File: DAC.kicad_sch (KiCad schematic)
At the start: 1 part, among them U401 MCP4728T-E_UN

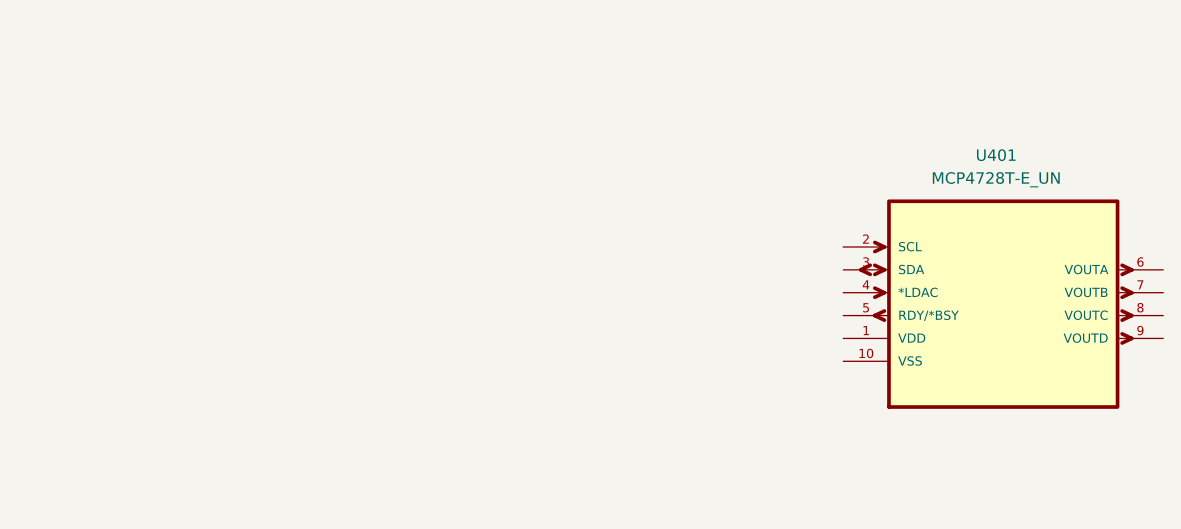
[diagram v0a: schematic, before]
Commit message: finished ADC side, may add some additional bare channels, started DAC part and need to add the tca0372 amplifier or think about it
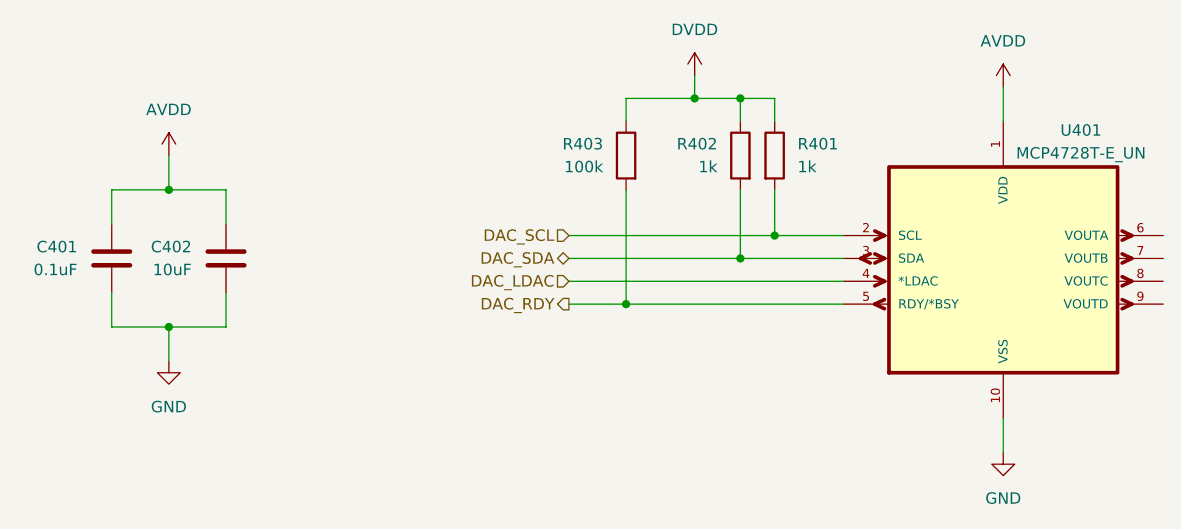
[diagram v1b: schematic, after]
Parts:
- added C401: 0.1uF, symbol Device:C
- added C402: 10uF, symbol Device:C
- added R401, R402: 1k, symbol Device:R
- added R403: 100k, symbol Device:R
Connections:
- net AVDD: now reaches U401.1 (VDD)
- net AVDD: now also C401.1, C402.1
- net GND: now reaches U401.10 (VSS)
- net GND: now also C401.2, C402.2
- net DAC_SCL: now reaches U401.2 (SCL)
- net DAC_SCL: now also R401.2
- net DAC_SDA: now reaches U401.3 (SDA)
- net DAC_SDA: now also R402.2
- net DAC_LDAC: now reaches U401.4 (*LDAC)
- net DAC_RDY: now reaches U401.5 (RDY/*BSY)
- net DAC_RDY: now also R403.2
- new net DVDD: R401.1, R402.1, R403.1
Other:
- moved on the sheet: U401

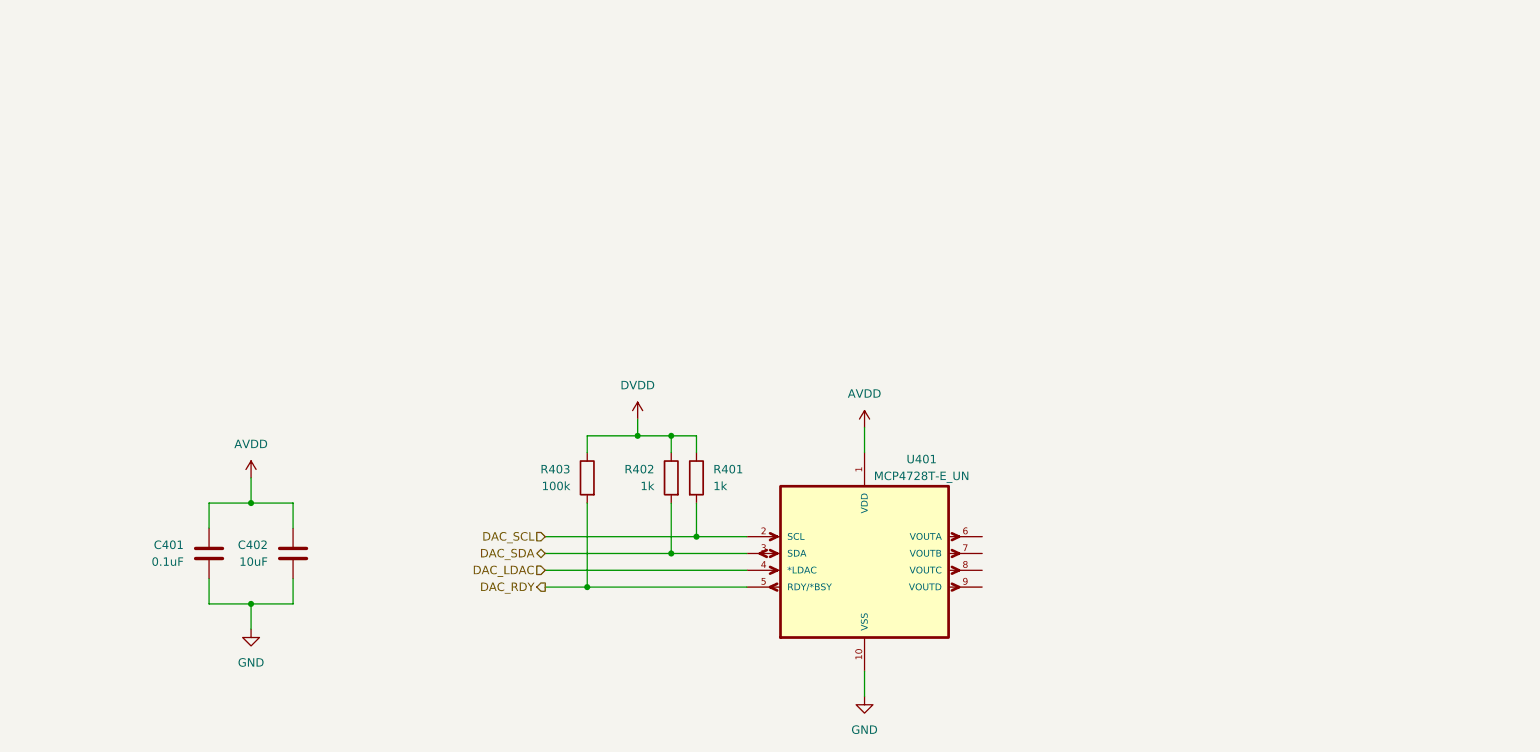
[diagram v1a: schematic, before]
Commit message: 80% done, maybe add more AINs, finish the power circuit and add system & block diagrams
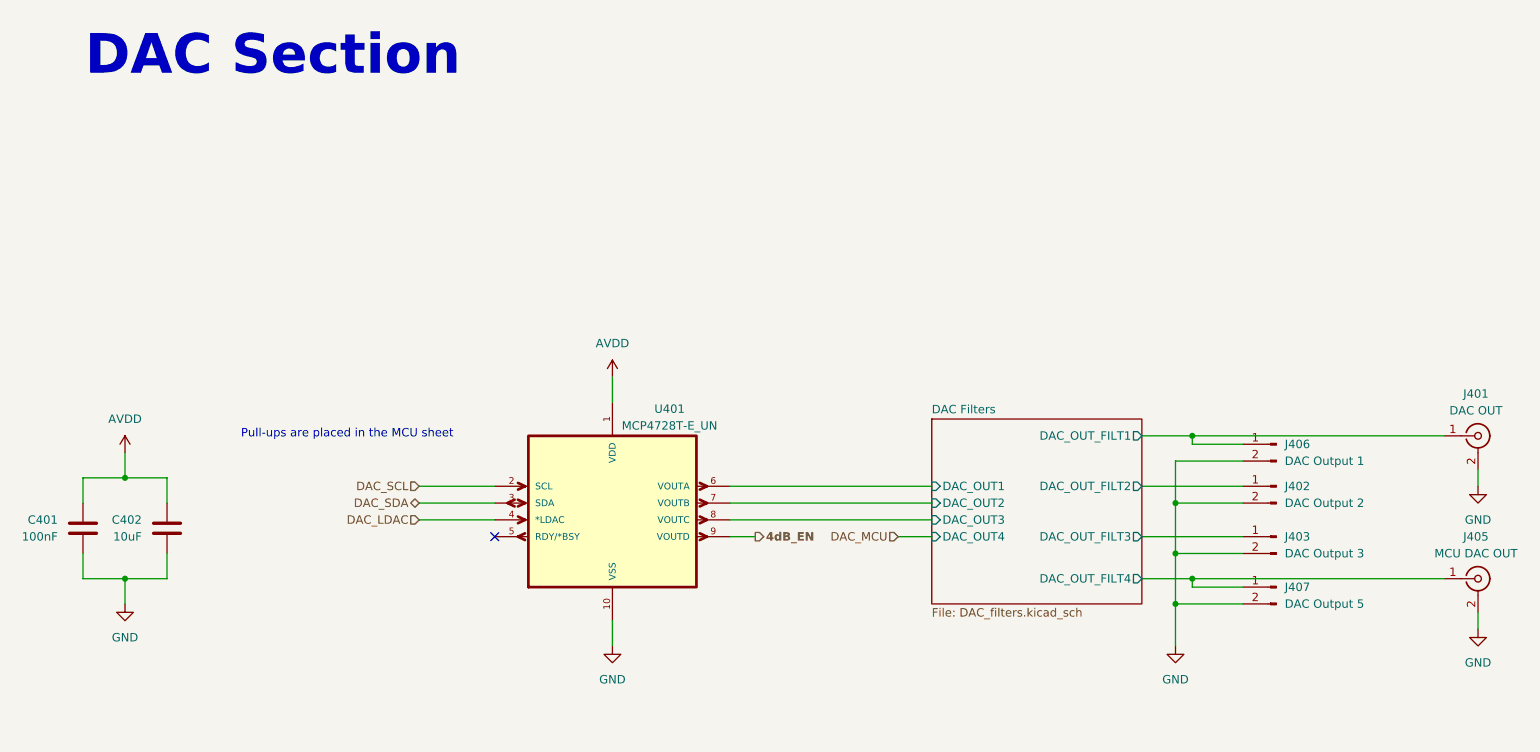
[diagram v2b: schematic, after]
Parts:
- removed R401, R402: 1k, symbol Device:R
- removed R403: 100k, symbol Device:R
- added J401: DAC OUT, symbol Connector:Conn_Coaxial
- added J402: DAC Output 2, symbol Connector:Conn_01x02_Pin
- added J403: DAC Output 3, symbol Connector:Conn_01x02_Pin
- added J405: MCU DAC OUT, symbol Connector:Conn_Coaxial
- added J406: DAC Output 1, symbol Connector:Conn_01x02_Pin
- added J407: DAC Output 5, symbol Connector:Conn_01x02_Pin
- C401: value 0.1uF -> 100nF
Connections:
- net GND: now also J401.2 (Ext), J402.2 (Pin_2), J403.2 (Pin_2), J405.2 (Ext), J406.2 (Pin_2), J407.2 (Pin_2)
- net DAC Filters/DAC_OUT1: now reaches U401.6 (VOUTA)
- net DAC Filters/DAC_OUT2: now reaches U401.7 (VOUTB)
- net DAC Filters/DAC_OUT3: now reaches U401.8 (VOUTC)
- net 4dB_EN: now reaches U401.9 (VOUTD)
- net DAC_RDY: no longer names the net of U401.5 (RDY/*BSY)
- new net DAC Filters/DAC_OUT_FILT1: J401.1 (In), J406.1 (Pin_1)
- new net DAC Filters/DAC_OUT_FILT2: J402.1 (Pin_1)
- new net DAC Filters/DAC_OUT_FILT3: J403.1 (Pin_1)
- new net DAC Filters/DAC_OUT_FILT4: J405.1 (In), J407.1 (Pin_1)
- no-connect marks 0 -> 1
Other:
- added sheet DAC Filters (DAC_filters.kicad_sch)
- note added: "DAC Section"
- note added: "Pull-ups are placed in the MCU sheet"
- moved on the sheet: C401, C402, U401

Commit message: finished individual block placement and started integrating, might need to change the AFEs length
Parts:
- C401: footprint (none) -> Capacitor_SMD:C_0603_1608Metric; MPN (none) -> 0603B104M250CT
- C402: footprint (none) -> Capacitor_SMD:C_0603_1608Metric; MPN (none) -> CL10A106MP8NNNC
- J401, J405: footprint (none) -> DOSIN-801-0083:CONN4_DOSIN-801_DOS; MPN (none) -> DOSIN-801-0083
- J402, J403, J406, J407: footprint (none) -> Connector_PinHeader_2.54mm:PinHeader_1x02_P2.54mm_Vertical; now not fitted
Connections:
- net 4dB_EN: no longer names the net of U401.9 (VOUTD)
- no-connect marks 1 -> 2
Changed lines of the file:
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@@
+	)
+	(no_connect
+		(at 120.65 95.25)
 	)
 	(no_connect
@@
 		(pts
 			(xy 120.65 92.71) (xy 151.13 92.71)
-		)
-		(stroke
-			(width 0)
-			(type default)
-		)
-	)
-	(wire
-		(pts
-			(xy 120.65 95.25) (xy 124.46 95.25)
 		)
 		(stroke
@@
 			)
 			(justify right)
-		)
-	)
-	(hierarchical_label "4dB_EN"
-		(shape output)
-		(at 124.46 95.25 0)
-		(effects
-			(font
-				(size 1.27 1.27)
-				(thickness 0.254)
-				(bold yes)
-			)
-			(justify left)
 		)
 	)
@@
 			)
 		)
-		(property "Footprint" ""
+		(property "Footprint" "DOSIN-801-0083:CONN4_DOSIN-801_DOS"
 			(at 233.68 101.6 0)
 			(effects
@@
 		)
 		(property "Description" "coaxial connector (BNC, SMA, SMB, SMC, Cinch/RCA, LEMO, ...)"
+			(at 233.68 101.6 0)
+			(effects
+				(font
+					(size 1.27 1.27)
+				)
+				(hide yes)
+			)
+		)
+		(property "MPN" "DOSIN-801-0083"
 			(at 233.68 101.6 0)
 			(effects
@@
 		(in_bom yes)
 		(on_board yes)
-		(dnp no)
+		(dnp yes)
 		(fields_autoplaced yes)
 		(property "Reference" "J407"
@@
 			)
 		)
-		(property "Footprint" ""
+		(property "Footprint" "Connector_PinHeader_2.54mm:PinHeader_1x02_P2.54mm_Vertical"
 			(at 203.2 102.87 0)
 			(effects
@@
 			)
 		)
-		(property "Footprint" ""
+		(property "Footprint" "Capacitor_SMD:C_0603_1608Metric"
 			(at 23.8252 97.79 0)
 			(effects
@@
 		)
 		(property "Description" "100nF 0603"
+			(at 22.86 93.98 0)
+			(effects
+				(font
+					(size 1.27 1.27)
+				)
+				(hide yes)
+			)
+		)
+		(property "MPN" "0603B104M250CT"
 			(at 22.86 93.98 0)
 			(effects
@@
 		(in_bom yes)
 		(on_board yes)
-		(dnp no)
+		(dnp yes)
 		(fields_autoplaced yes)
 		(property "Reference" "J403"
@@
 			)
 		)
-		(property "Footprint" ""
+		(property "Footprint" "Connector_PinHeader_2.54mm:PinHeader_1x02_P2.54mm_Vertical"
 			(at 203.2 95.25 0)
 			(effects
@@
 			)
 		)
-		(property "Footprint" ""
+		(property "Footprint" "DOSIN-801-0083:CONN4_DOSIN-801_DOS"
 			(at 233.68 80.01 0)
 			(effects
@@
 		)
 		(property "Description" "coaxial connector (BNC, SMA, SMB, SMC, Cinch/RCA, LEMO, ...)"
+			(at 233.68 80.01 0)
+			(effects
+				(font
+					(size 1.27 1.27)
+				)
+				(hide yes)
+			)
+		)
+		(property "MPN" "DOSIN-801-0083"
 			(at 233.68 80.01 0)
 			(effects
@@
 				(path "/eb93e2be-0074-48a1-b88c-5129bddcbd28/1b72d40f-f387-447e-822a-04789696d01d"
 					(reference "J401")
-					(unit 1)
-				)
-			)
-		)
-	)
-	(symbol
-		(lib_id "power:+5V")
-		(at 102.87 71.12 0)
-		(unit 1)
-		(exclude_from_sim no)
-		(in_bom yes)
-		(on_board yes)
-		(dnp no)
-		(fields_autoplaced yes)
-		(property "Reference" "#PWR0402"
-			(at 102.87 74.93 0)
-			(effects
-				(font
-					(size 1.27 1.27)
-				)
-				(hide yes)
-			)
-		)
-		(property "Value" "AVDD"
-			(at 102.87 66.04 0)
-			(effects
-				(font
-					(size 1.27 1.27)
-				)
-			)
-		)
-		(property "Footprint" ""
-			(at 102.87 71.12 0)
-			(effects
-				(font
-					(size 1.27 1.27)
-				)
-				(hide yes)
-			)
-		)
-		(property "Datasheet" ""
-			(at 102.87 71.12 0)
-			(effects
-				(font
-					(size 1.27 1.27)
-				)
-				(hide yes)
-			)
-		)
-		(property "Description" "Power symbol creates a global label with name \"AVDD\""
-			(at 102.87 71.12 0)
-			(effects
-				(font
-					(size 1.27 1.27)
-				)
-				(hide yes)
-			)
-		)
-		(pin "1"
-		)
-		(instances
-			(project "NadyScope"
-				(path "/eb93e2be-0074-48a1-b88c-5129bddcbd28/1b72d40f-f387-447e-822a-04789696d01d"
-					(reference "#PWR0402")
 					(unit 1)
 				)
@@
 			)
 		)
-		(property "Footprint" ""
+		(property "Footprint" "Capacitor_SMD:C_0603_1608Metric"
 			(at 36.5252 97.79 0)
 			(effects
@@
 		)
 		(property "Description" "1uF 0603"
+			(at 35.56 93.98 0)
+			(effects
+				(font
+					(size 1.27 1.27)
+				)
+				(hide yes)
+			)
+		)
+		(property "MPN" "CL10A106MP8NNNC"
 			(at 35.56 93.98 0)
 			(effects
@@
 		(in_bom yes)
 		(on_board yes)
-		(dnp no)
+		(dnp yes)
 		(fields_autoplaced yes)
 		(property "Reference" "J406"
@@
 			)
 		)
-		(property "Footprint" ""
+		(property "Footprint" "Connector_PinHeader_2.54mm:PinHeader_1x02_P2.54mm_Vertical"
 			(at 203.2 81.28 0)
 			(effects
@@
 	)
 	(symbol
+		(lib_id "power:+3.3V")
+		(at 102.87 71.12 0)
+		(unit 1)
+		(exclude_from_sim no)
+		(in_bom yes)
+		(on_board yes)
+		(dnp no)
+		(fields_autoplaced yes)
+		(property "Reference" "#PWR0402"
+			(at 102.87 74.93 0)
+			(effects
+				(font
+					(size 1.27 1.27)
+				)
+				(hide yes)
+			)
+		)
+		(property "Value" "AVDD"
+			(at 102.87 66.04 0)
+			(effects
+				(font
+					(size 1.27 1.27)
+				)
+			)
+		)
+		(property "Footprint" ""
+			(at 102.87 71.12 0)
+			(effects
+				(font
+					(size 1.27 1.27)
+				)
+				(hide yes)
+			)
+		)
+		(property "Datasheet" ""
+			(at 102.87 71.12 0)
+			(effects
+				(font
+					(size 1.27 1.27)
+				)
+				(hide yes)
+			)
+		)
+		(property "Description" "Power symbol creates a global label with name \"AVDD\""
+			(at 102.87 71.12 0)
+			(effects
+				(font
+					(size 1.27 1.27)
+				)
+				(hide yes)
+			)
+		)
+		(pin "1"
+		)
+		(instances
+			(project "NadyScope"
+				(path "/eb93e2be-0074-48a1-b88c-5129bddcbd28/1b72d40f-f387-447e-822a-04789696d01d"
+					(reference "#PWR0402")
+					(unit 1)
+				)
+			)
+		)
+	)
+	(symbol
 		(lib_id "Connector:Conn_01x02_Pin")
 		(at 203.2 87.63 0)
@@
 		(in_bom yes)
 		(on_board yes)
-		(dnp no)
+		(dnp yes)
 		(fields_autoplaced yes)
 		(property "Reference" "J402"
@@
 			)
 		)
-		(property "Footprint" ""
+		(property "Footprint" "Connector_PinHeader_2.54mm:PinHeader_1x02_P2.54mm_Vertical"
 			(at 203.2 87.63 0)
 			(effects
